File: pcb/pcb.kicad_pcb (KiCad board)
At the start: 2 copper layers, 60 x 35 mm, 20 parts, among them J1 Conn_01x09_Pin, J2 Conn_01x09_Pin, J3 Conn_01x09_Pin, J4 Conn_01x09_Pin, J5 Conn_01x04_Pin, J6 Conn_01x04_Pin, J9 Conn_01x09_Pin

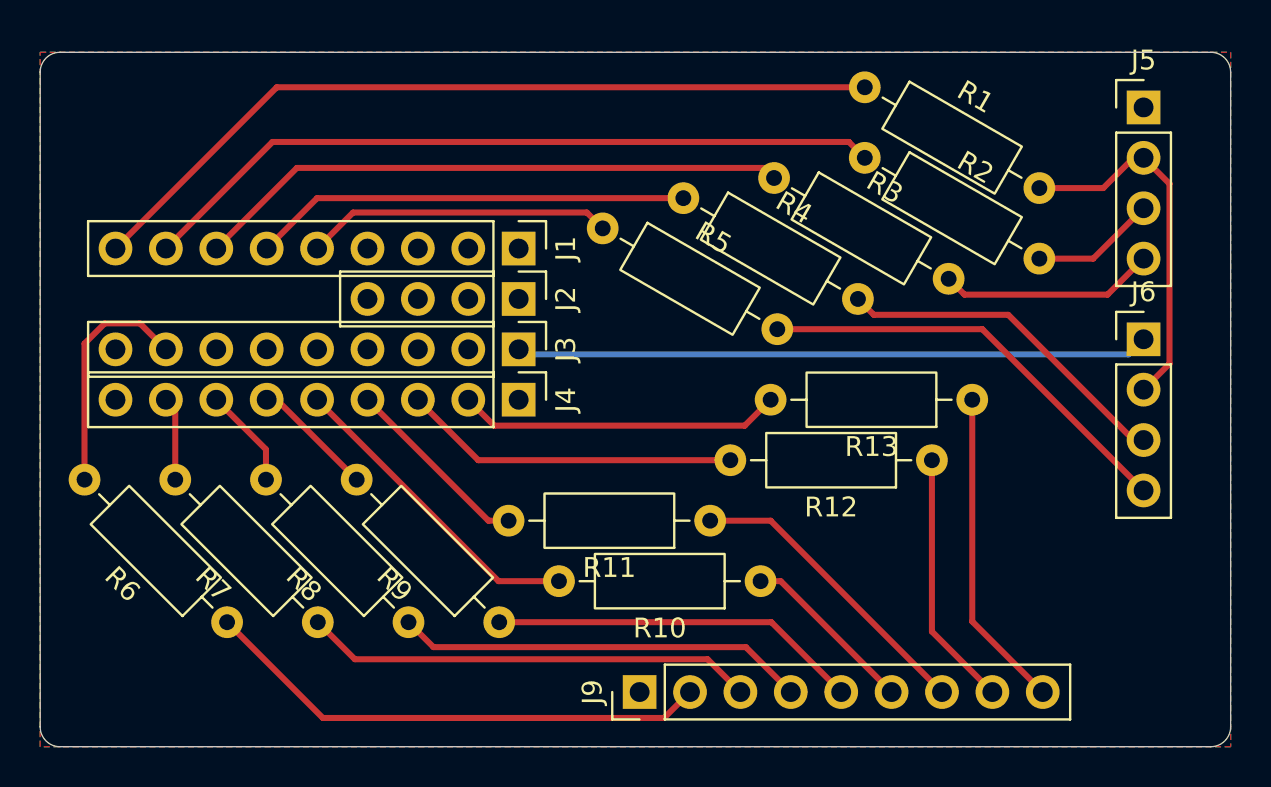
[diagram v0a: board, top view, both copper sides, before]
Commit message: chore: reorganise resistors and wire paths
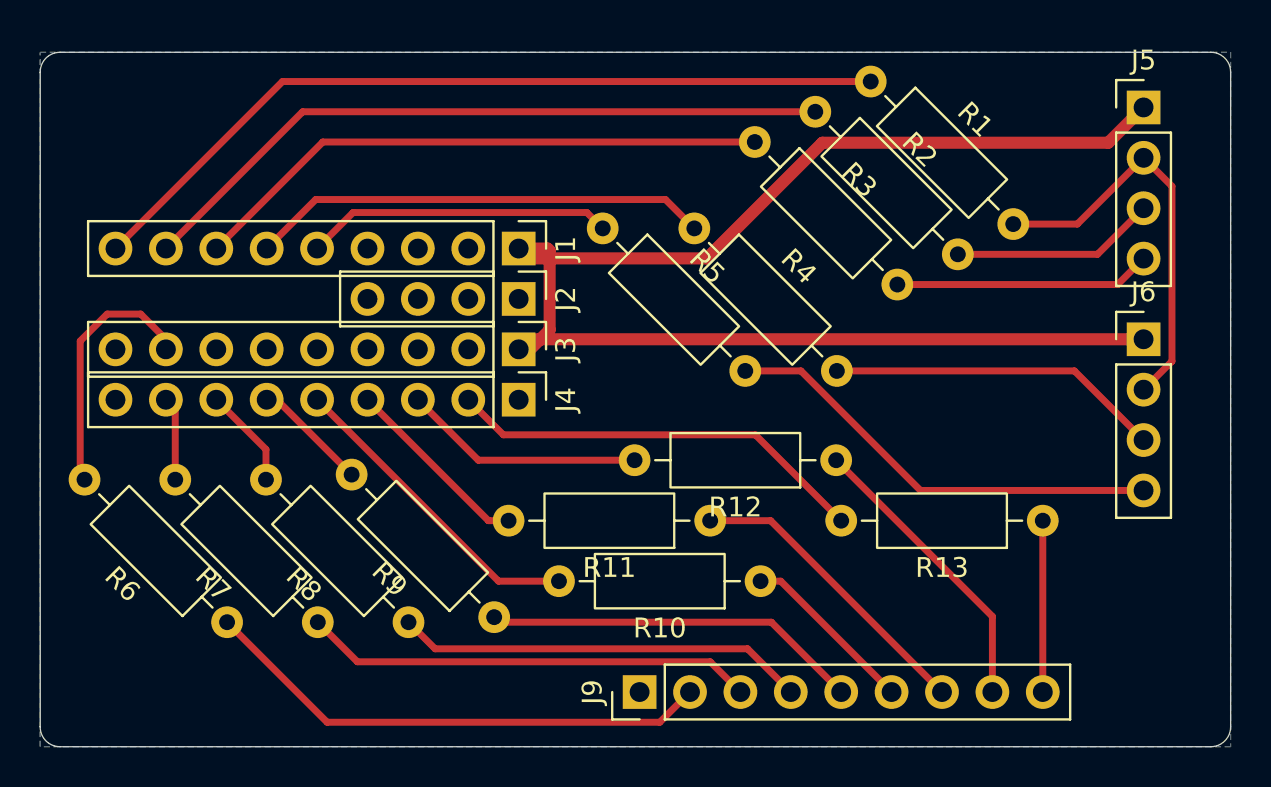
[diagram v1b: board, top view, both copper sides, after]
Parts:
- moved R13 7.06 mm to (65.5, 38.6)
- moved R12 4.83 mm to (55.1, 35.6)
- moved R2 3.41 mm to (54.1, 18.0), turned to -45 degrees
- moved R3 2.06 mm to (51.0, 19.5), turned to -45 degrees
- moved R4 1.62 mm to (48.0, 23.9), turned to -45 degrees
- moved R1 0.42 mm to (56.9, 16.5), turned to -45 degrees
- moved R9 0.36 mm to (37.9, 43.5)
- turned R5 to -45 degrees
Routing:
- net +3V3: track 31.9 -> 74.1 mm
- net Net-(J9-Pin_9): track 16.2 -> 8.64 mm
- net /B.2: track 16.3 -> 21.3 mm
- net /B.5: track 17.0 -> 12.2 mm
- net Net-(J5-Pin_3): track 6.30 -> 10.3 mm
- net /B.30: track 37.8 -> 35.6 mm
- net Net-(J5-Pin_2): track 18.7 -> 20.8 mm
- net Net-(J5-Pin_4): track 10.9 -> 13.0 mm
- net Net-(J9-Pin_8): track 12.9 -> 14.9 mm
- net Net-(J6-Pin_3): track 18.0 -> 16.9 mm
- net /B.36: track 22.1 -> 23.2 mm
- net /B.21: track 11.9 -> 13.0 mm
- net Net-(J6-Pin_4): track 21.8 -> 22.6 mm
- net /B.33: track 30.0 -> 29.4 mm
- removed copper zone on F.Cu, net +3V3
